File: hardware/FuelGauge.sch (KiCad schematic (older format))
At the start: 38 parts

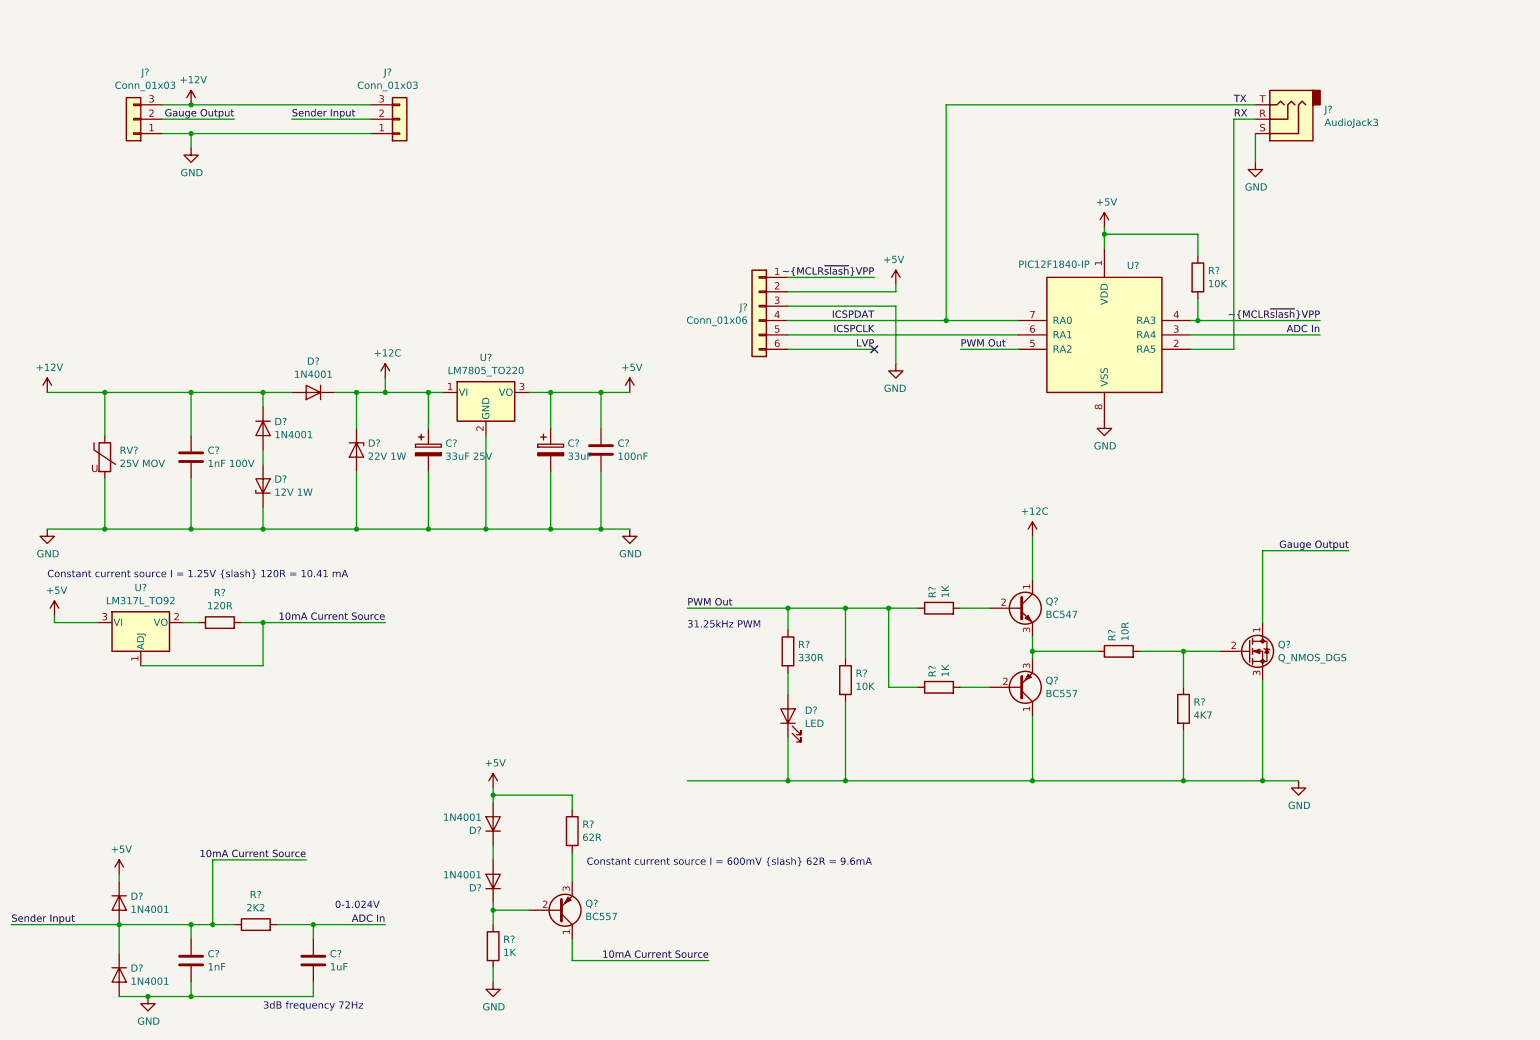
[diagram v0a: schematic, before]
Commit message: Feature complete HW design with hack PCB layout
This completes the HW after testing on a breadboard. Both the
sender input and gauge output have been tested.

A fuel low output has been hacked together though this has no
software currently and may be replaced with a 12V indicator.

The PCB layout is functional and passes DRC but is pretty awful
otherwise.

Tests:
 - Run clean run of ERC on the schematics and DRC on the PCB.
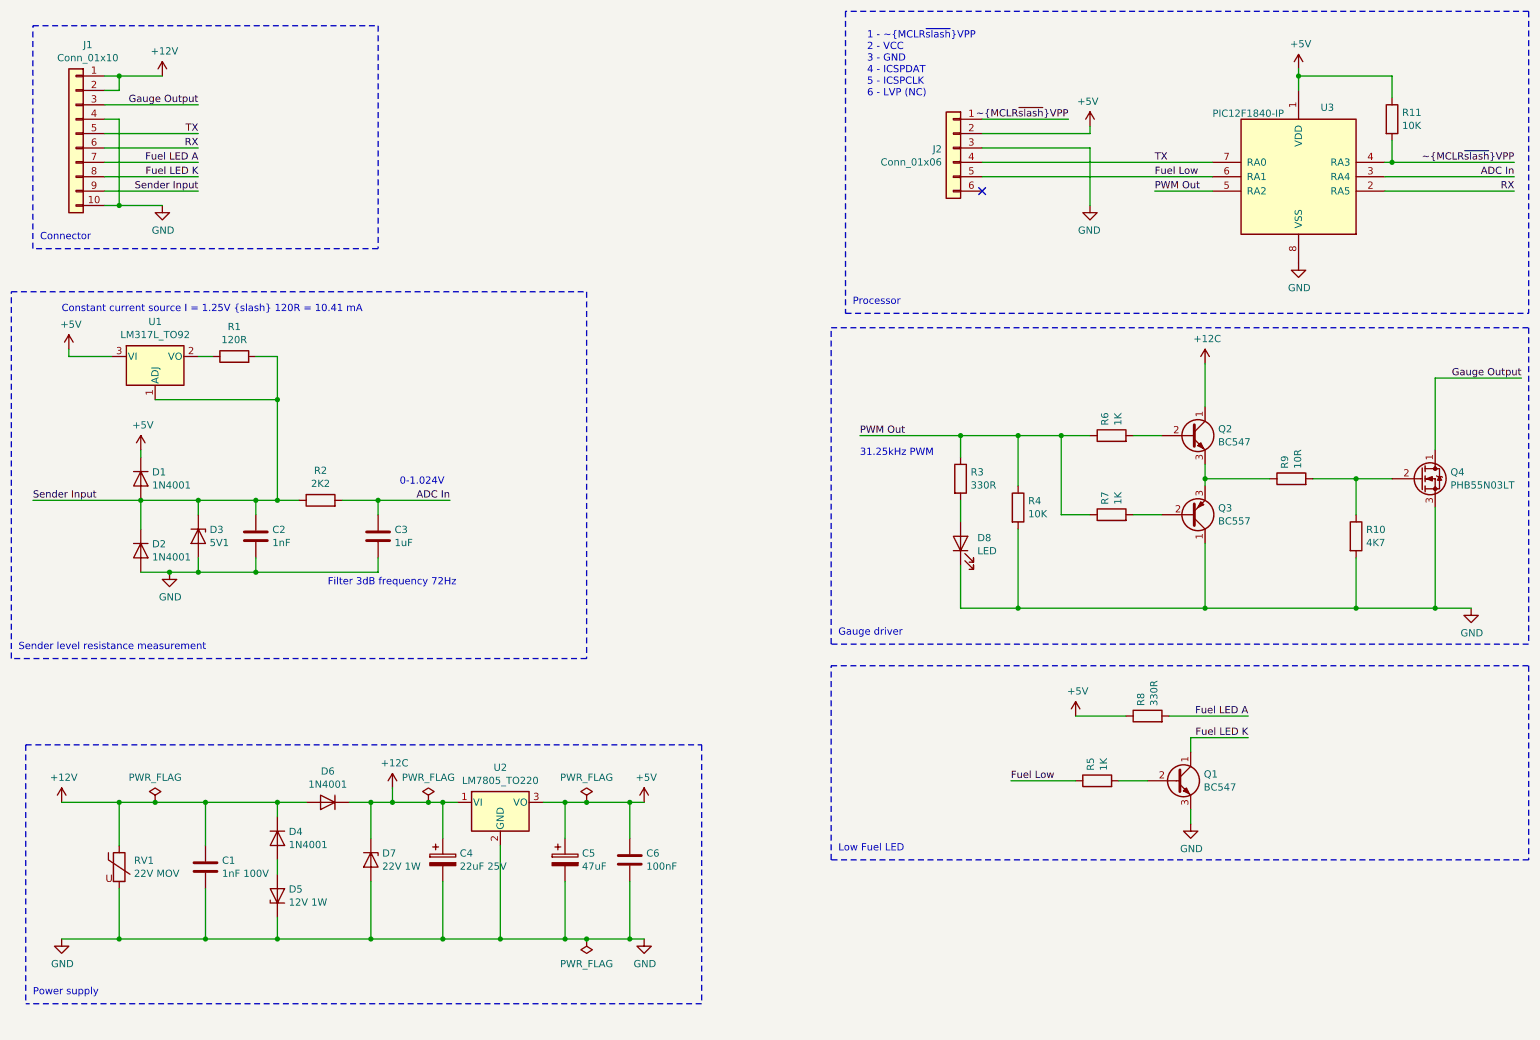
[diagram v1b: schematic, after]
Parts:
- removed D? (x2): 1N4001, symbol Device:D
- removed J? (x2): Conn_01x03, symbol Connector_Generic:Conn_01x03
- removed J?: AudioJack3, symbol Connector:AudioJack3
- removed Q?: BC557, Package_TO_SOT_THT:TO-92_Inline, symbol Transistor_BJT:BC557
- removed R?: 1K, symbol Device:R
- removed R?: 62R, symbol Device:R
- removed R?: 10K, symbol Device:R
- removed U?: LM7805_TO220, Package_TO_SOT_THT:TO-220-3_Vertical, symbol Regulator_Linear:LM7805_TO220
- added D3: 5V1, Diode_THT:D_DO-41_SOD81_P10.16mm_Horizontal, symbol Device:D_Zener
- added J1: Conn_01x10, Connector_Molex:Molex_KK-254_AE-6410-10A_1x10_P2.54mm_Vertical, symbol Connector_Generic:Conn_01x10
- added Q1: BC547, Package_TO_SOT_THT:TO-92_Inline, symbol Transistor_BJT:BC547
- added R11: 10K, Resistor_THT:R_Axial_DIN0207_L6.3mm_D2.5mm_P10.16mm_Horizontal, symbol Device:R
- added R5: 1K, Resistor_THT:R_Axial_DIN0207_L6.3mm_D2.5mm_P10.16mm_Horizontal, symbol Device:R
- added R8: 330R, Resistor_THT:R_Axial_DIN0207_L6.3mm_D2.5mm_P10.16mm_Horizontal, symbol Device:R
- added U2: LM7805_TO220, Package_TO_SOT_THT:TO-220-3_Vertical, symbol Regulator_Linear:LM7805_TO220
- C1, C3: renamed from C?; footprint (none) -> Capacitor_THT:C_Rect_L7.0mm_W6.0mm_P5.00mm
- C2: renamed from C?; footprint (none) -> Capacitor_THT:C_Disc_D3.0mm_W1.6mm_P2.50mm
- C4: renamed from C?; value 33uF 25V -> 22uF 25V; footprint (none) -> Capacitor_THT:CP_Radial_D5.0mm_P2.00mm
- C5: renamed from C?; value 33uF -> 47uF; footprint (none) -> Capacitor_THT:CP_Radial_Tantal_D6.0mm_P5.00mm
- C6: renamed from C?; footprint (none) -> Capacitor_THT:C_Disc_D3.4mm_W2.1mm_P2.50mm
- D1, D2, D4, D5, D6, D7: renamed from D?; footprint (none) -> Diode_THT:D_DO-41_SOD81_P10.16mm_Horizontal
- D8: renamed from D?; footprint (none) -> LED_THT:LED_D5.0mm_Clear
- J2: renamed from J?; footprint (none) -> Connector_PinHeader_2.54mm:PinHeader_1x06_P2.54mm_Vertical
- Q4: renamed from Q?; value Q_NMOS_DGS -> PHB55N03LT; footprint (none) -> Package_TO_SOT_SMD:TO-263-3_TabPin2
- R1, R10, R2, R3, R4, R6, R7, R9: renamed from R?; footprint (none) -> Resistor_THT:R_Axial_DIN0207_L6.3mm_D2.5mm_P10.16mm_Horizontal
- RV1: renamed from RV?; value 25V MOV -> 22V MOV; footprint (none) -> Varistor:RV_Disc_D7mm_W3.4mm_P5mm
- gave numbers to parts that had none: 4
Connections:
- net +12C: now also U2.1 (VI)
- net +12V: now also J1.1 (Pin_1), J1.2 (Pin_2)
- net +5V: now also R11.1, R8.1, U2.3 (VO)
- net GND: now also D3.2 (A), J1.10 (Pin_10), J1.4 (Pin_4), Q1.3 (E), U2.2 (GND)
- net Gauge Output: now also J1.3 (Pin_3)
- net RX: now also J1.6 (Pin_6)
- net ~MCLR~/VPP: now also R11.2
- net 10mA Current Source renamed Sender Input
- net Sender Input: now also D3.1 (K), J1.9 (Pin_9)
- net ICSPCLK renamed Fuel Low
- net Fuel Low: now also R5.1
- net ICSPDAT renamed TX
- net TX: now also J1.5 (Pin_5)
- net LVP: no longer names the net of J2.6 (Pin_6)
- new net: Q1.2 (B), R5.2
- new net Fuel LED A: J1.7 (Pin_7), R8.2
- new net Fuel LED K: J1.8 (Pin_8), Q1.1 (C)
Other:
- note added: "1 - ~MCLR~/VPP\n2 - VCC\n3 - GND\n4 - ICSPDAT\n5 - ICSPCLK\n6 - LVP (NC)"
- note added: "Connector"
- note added: "Filter 3dB frequency 72Hz"
- note added: "Gauge driver"
- note added: "Low Fuel LED"
- note added: "Power supply"
- note added: "Processor"
- note added: "Sender level resistance measurement"
- note removed: "3dB frequency 72Hz"
- note removed: "Constant current source I = 600mV / 62R = 9.6mA"
- moved on the sheet: C1, C2, C3, C4, C5, C6, D1, D2, D4, D5, D6, D7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

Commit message: Version 1.0 hardware
This change contains what is hoped to be 1.0 hardware. It removes the complex MOSFET driver for a simple direct drive
from the MCU. The LED has been removed as this appears to
provide little value as the VDO test guage uses 65% to 98% duty
cycle to cover 0% to 100% which is virtually imperceptible.

A simple transistor driver for a low fuel warning LED or lamp has
been included. This should work with a 12V LED indicator lamp.

Tests:
 - Run a full ERC on schematic and DRC on the PCB
 - Check mechanical fit with a 1:1 printout against the Hammond
   1691ABK case
 - Check new MOSFET driver with VDO fuel gauge and calibrate
   output map. MOSFET turn on time seems to be about 1uS
   which should be OK given low current.
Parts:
- removed D8: LED, LED_THT:LED_D5.0mm_Clear, symbol Device:LED
- removed Q2: BC547, Package_TO_SOT_THT:TO-92_Inline, symbol Transistor_BJT:BC547
- removed Q3: BC557, Package_TO_SOT_THT:TO-92_Inline, symbol Transistor_BJT:BC557
- removed Q4: PHB55N03LT, Package_TO_SOT_SMD:TO-263-3_TabPin2, symbol Device:Q_NMOS_DGS
- removed R3, R8: 330R, Resistor_THT:R_Axial_DIN0207_L6.3mm_D2.5mm_P10.16mm_Horizontal, symbol Device:R
- removed R4: 10K, Resistor_THT:R_Axial_DIN0207_L6.3mm_D2.5mm_P10.16mm_Horizontal, symbol Device:R
- removed R6, R7: 1K, Resistor_THT:R_Axial_DIN0207_L6.3mm_D2.5mm_P10.16mm_Horizontal, symbol Device:R
- added Q2: PHB55N03LT, Package_TO_SOT_SMD:TO-263-3_TabPin2, symbol Device:Q_NMOS_GDS
- U2: footprint Package_TO_SOT_THT:TO-220-3_Vertical -> Package_TO_SOT_THT:TO-220-3_Horizontal_TabDown
- renumbered R5 to R3, R9 to R4, R10 to R5, R11 to R6
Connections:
- net Fuel LED A is gone; now on net RX: J1.7 (Pin_7)
- net +12V: now also J1.4 (Pin_4), J1.5 (Pin_5); no longer J1.1 (Pin_1), J1.2 (Pin_2)
- net GND: now also J1.2 (Pin_2), J1.8 (Pin_8), Q2.3 (S); no longer J1.4 (Pin_4)
- net Gauge Output: now also J1.1 (Pin_1), Q2.2 (D); no longer J1.3 (Pin_3)
- net PWM Out: now also R4.1
- net RX: no longer J1.6 (Pin_6)
- net TX: now also J1.6 (Pin_6); no longer J1.5 (Pin_5)
- net at R4.2, R5.1: now also Q2.1 (G)
- net +12C: no longer names the net of C4.1, D6.1 (K), D7.1 (K), U2.1 (VI)
- net Fuel LED K renamed Fuel Low Output
- net Fuel Low Output: now also J1.3 (Pin_3); no longer J1.8 (Pin_8)
